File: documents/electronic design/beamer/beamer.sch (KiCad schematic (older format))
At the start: 25 parts, among them P1 CONN_01X20, P2 CONN_01X20, T1 2N7002K, T10 2N7002K, T2 2N7002K, T3 2N7002K, T4 2N7002K, T5 2N7002K, T6 2N7002K, T7 2N7002K, T8 2N7002K, T9 2N7002K, U1 NRF24L01-BRKOUT, U2 74HC595D

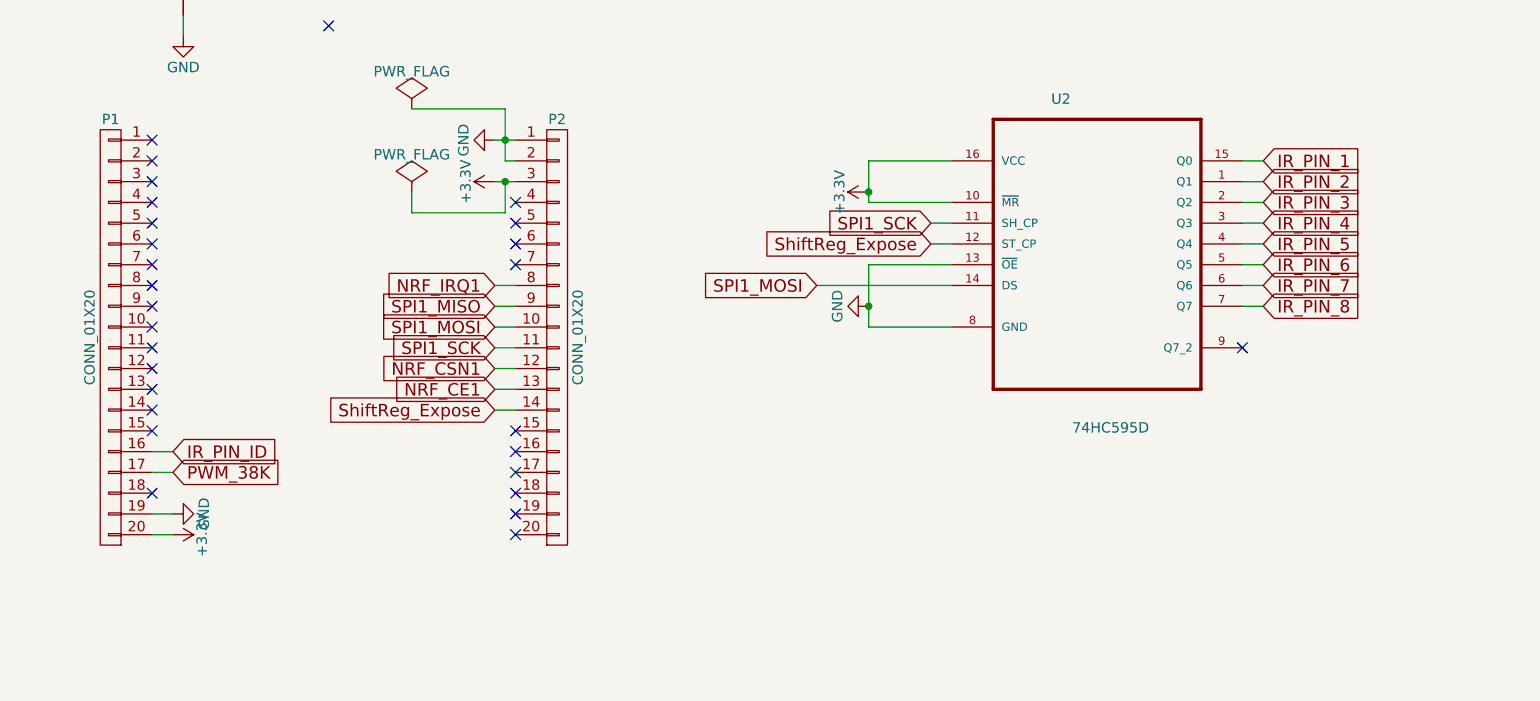
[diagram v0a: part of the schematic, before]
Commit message: update pcb for beamer with shift registar
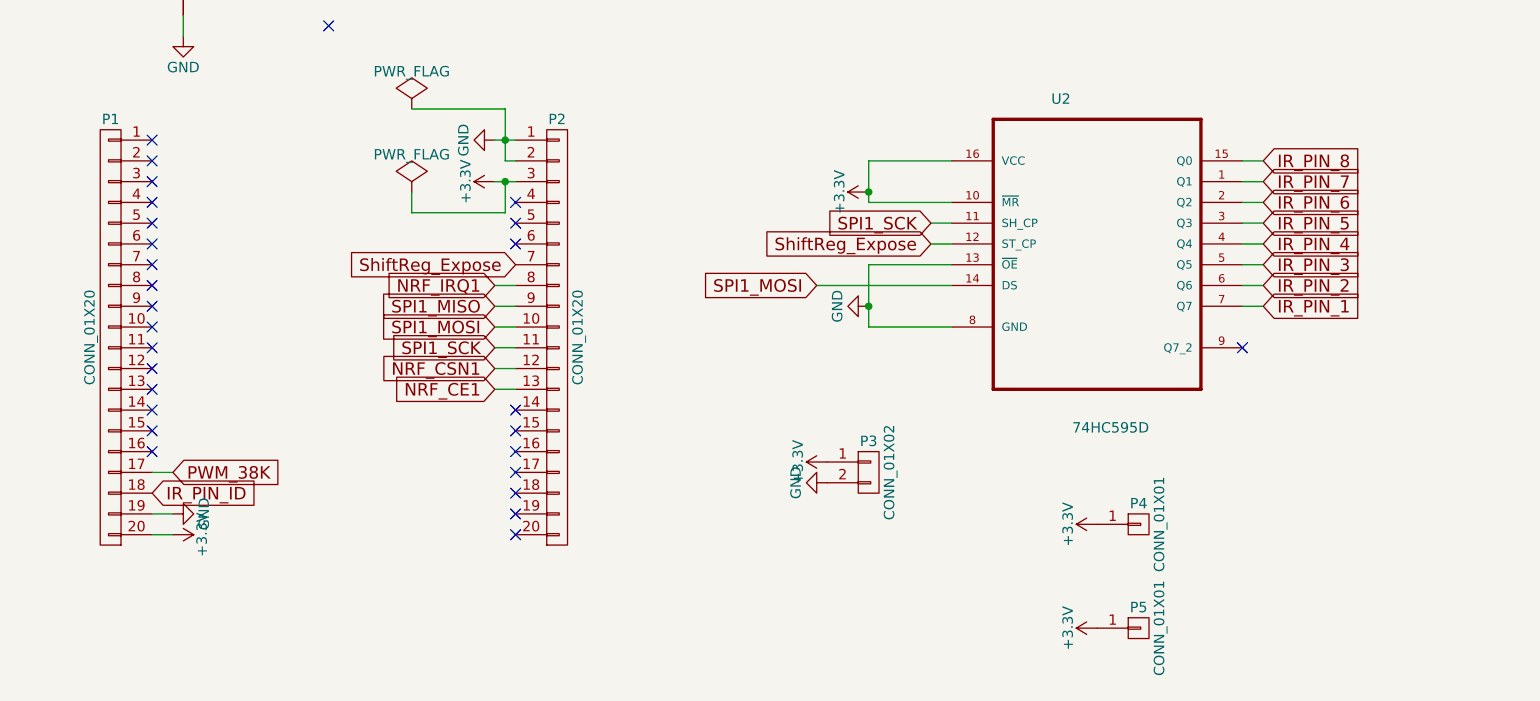
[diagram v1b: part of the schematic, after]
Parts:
- added P3: CONN_01X02, Pin_Headers:Pin_Header_Straight_1x02, symbol CONN_01X02
- added P4, P5: CONN_01X01, Pin_Headers:Pin_Header_Straight_1x01, symbol CONN_01X01
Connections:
- net +3V3: now also P3.1 (P1), P4.1 (P1), P5.1 (P1)
- net GND: now also P3.2 (P2)
- net IR_PIN_1: now also U2.7 (Q7); no longer U2.15 (Q0)
- net IR_PIN_2: now also U2.6 (Q6); no longer U2.1 (Q1)
- net IR_PIN_3: now also U2.5 (Q5); no longer U2.2 (Q2)
- net IR_PIN_4: now also U2.4 (Q4); no longer U2.3 (Q3)
- net IR_PIN_5: now also U2.3 (Q3); no longer U2.4 (Q4)
- net IR_PIN_6: now also U2.2 (Q2); no longer U2.5 (Q5)
- net IR_PIN_7: now also U2.1 (Q1); no longer U2.6 (Q6)
- net IR_PIN_8: now also U2.15 (Q0); no longer U2.7 (Q7)
- net IR_PIN_ID: now also P1.18 (P18); no longer P1.16 (P16)
- net ShiftReg_Expose: now also P2.7 (P7); no longer P2.14 (P14)
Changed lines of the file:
@@
 Text GLabel 4450 4300 0    60   Input ~ 0
 NRF_IRQ1
+Text GLabel 8150 4400 2    60   Input ~ 0
+IR_PIN_1
+Text GLabel 8150 4300 2    60   Input ~ 0
+IR_PIN_2
+Text GLabel 8150 4200 2    60   Input ~ 0
+IR_PIN_3
+Text GLabel 8150 4100 2    60   Input ~ 0
+IR_PIN_4
+Text GLabel 8150 4000 2    60   Input ~ 0
+IR_PIN_5
+Text GLabel 8150 3900 2    60   Input ~ 0
+IR_PIN_6
+Text GLabel 8150 3800 2    60   Input ~ 0
+IR_PIN_7
 Text GLabel 8150 3700 2    60   Input ~ 0
-IR_PIN_1
-Text GLabel 8150 3800 2    60   Input ~ 0
-IR_PIN_2
-Text GLabel 8150 3900 2    60   Input ~ 0
-IR_PIN_3
-Text GLabel 8150 4000 2    60   Input ~ 0
-IR_PIN_4
-Text GLabel 8150 4100 2    60   Input ~ 0
-IR_PIN_5
-Text GLabel 8150 4200 2    60   Input ~ 0
-IR_PIN_6
-Text GLabel 8150 4300 2    60   Input ~ 0
-IR_PIN_7
-Text GLabel 8150 4400 2    60   Input ~ 0
 IR_PIN_8
-Text GLabel 2900 5100 2    60   Input ~ 0
+Text GLabel 2800 5300 2    60   Input ~ 0
 IR_PIN_ID
-NoConn ~ 2800 5300
 NoConn ~ 2800 4200
 NoConn ~ 2800 4100
@@
 	1    0    0    -1
 $EndComp
-NoConn ~ 4550 4200
 NoConn ~ 2800 3600
 $Comp
@@
 	4450 3800 4550 3800
 Wire Wire Line
-	2800 5100 2900 5100
-Wire Wire Line
 	8050 4400 8150 4400
 Wire Wire Line
@@
 Wire Wire Line
 	6550 4000 6650 4000
-Text GLabel 4450 4900 0    60   Input ~ 0
+Text GLabel 4550 4200 0    60   Input ~ 0
 ShiftReg_Expose
 Text GLabel 6550 4100 0    60   Input ~ 0
@@
 NoConn ~ 4550 5100
 NoConn ~ 3650 3050
-Wire Wire Line
-	4550 4900 4450 4900
 NoConn ~ 2800 5000
+$Comp
+L CONN_01X02 P3
+U 1 1 57685656
+P 6250 5200
+F 0 "P3" H 6250 5350 50  0000 C CNN
+F 1 "CONN_01X02" V 6350 5200 50  0000 C CNN
+F 2 "Pin_Headers:Pin_Header_Straight_1x02" H 6250 5200 50  0001 C CNN
+F 3 "" H 6250 5200 50  0000 C CNN
+	1    6250 5200
+	1    0    0    -1
+$EndComp
+$Comp
+L +3.3V #PWR013
+U 1 1 5768570E
+P 6050 5150
+F 0 "#PWR013" H 6050 5000 50  0001 C CNN
+F 1 "+3.3V" H 6050 5290 50  0000 C CNN
+F 2 "" H 6050 5150 50  0000 C CNN
+F 3 "" H 6050 5150 50  0000 C CNN
+	1    6050 5150
+	0    -1   -1   0
+$EndComp
+$Comp
+L GND #PWR014
+U 1 1 57685767
+P 6050 5250
+F 0 "#PWR014" H 6050 5000 50  0001 C CNN
+F 1 "GND" H 6050 5100 50  0000 C CNN
+F 2 "" H 6050 5250 50  0000 C CNN
+F 3 "" H 6050 5250 50  0000 C CNN
+	1    6050 5250
+	0    1    1    0
+$EndComp
+NoConn ~ 4550 4900
+$Comp
+L CONN_01X01 P4
+U 1 1 5768633C
+P 7550 5450
+F 0 "P4" H 7550 5550 50  0000 C CNN
+F 1 "CONN_01X01" V 7650 5450 50  0000 C CNN
+F 2 "Pin_Headers:Pin_Header_Straight_1x01" H 7550 5450 50  0001 C CNN
+F 3 "" H 7550 5450 50  0000 C CNN
+	1    7550 5450
+	1    0    0    -1
+$EndComp
+$Comp
+L CONN_01X01 P5
+U 1 1 576863D4
+P 7550 5950
+F 0 "P5" H 7550 6050 50  0000 C CNN
+F 1 "CONN_01X01" V 7650 5950 50  0000 C CNN
+F 2 "Pin_Headers:Pin_Header_Straight_1x01" H 7550 5950 50  0001 C CNN
+F 3 "" H 7550 5950 50  0000 C CNN
+	1    7550 5950
+	1    0    0    -1
+$EndComp
+$Comp
+L +3.3V #PWR015
+U 1 1 5768645D
+P 7350 5450
+F 0 "#PWR015" H 7350 5300 50  0001 C CNN
+F 1 "+3.3V" H 7350 5590 50  0000 C CNN
+F 2 "" H 7350 5450 50  0000 C CNN
+F 3 "" H 7350 5450 50  0000 C CNN
+	1    7350 5450
+	0    -1   -1   0
+$EndComp
+$Comp
+L +3.3V #PWR016
+U 1 1 576864BF
+P 7350 5950
+F 0 "#PWR016" H 7350 5800 50  0001 C CNN
+F 1 "+3.3V" H 7350 6090 50  0000 C CNN
+F 2 "" H 7350 5950 50  0000 C CNN
+F 3 "" H 7350 5950 50  0000 C CNN
+	1    7350 5950
+	0    -1   -1   0
+$EndComp
+NoConn ~ 2800 5100
 $EndSCHEMATC

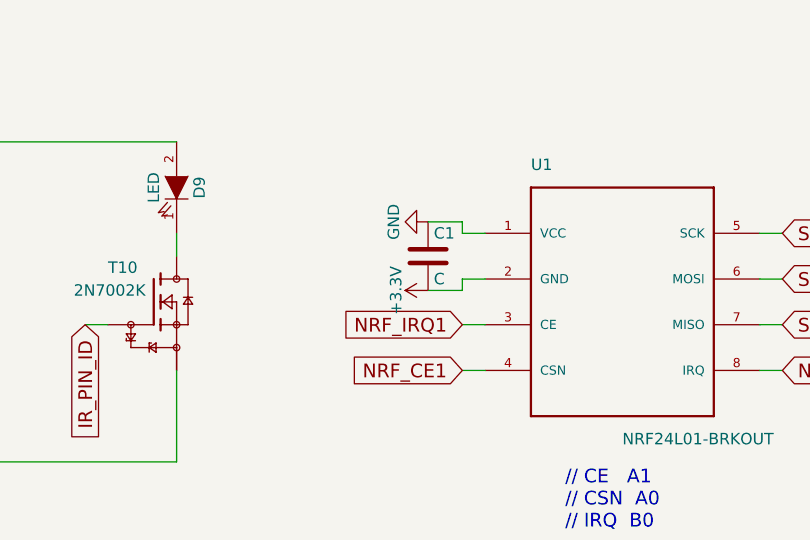
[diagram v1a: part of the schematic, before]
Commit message: update PCB for beamer, fix pin assignment for radiomodule
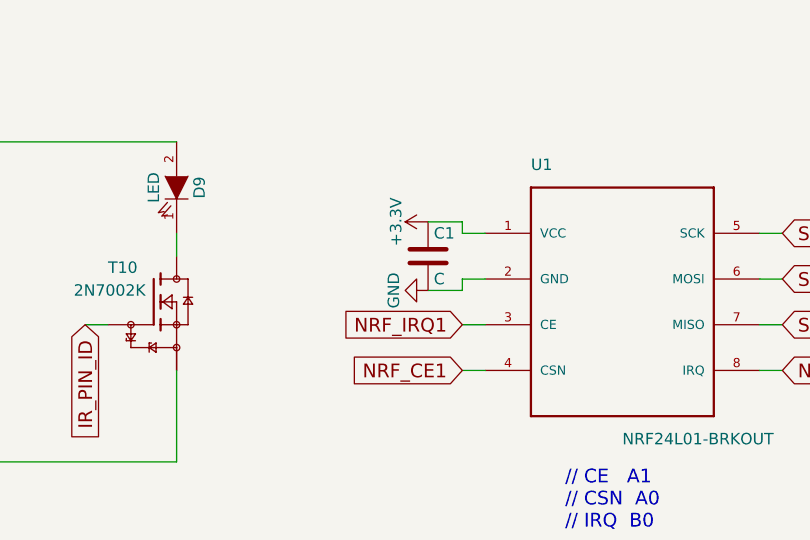
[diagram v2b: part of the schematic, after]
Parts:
- T1, T10, T2, T3, T4, T5, T6, T7, T8, T9: footprint sot23_modified:SOT23Mod -> sot23_modified:SOT23
- U1: footprint se8r01_smd:SE8R01_SMD -> NRF24L01-BRKOUT:NRF24L01-BKKOUT
- U2: footprint SOIC127P1030X265-16N:SOIC127P1030X265-16N -> 74HC595:SO16
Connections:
- net +3V3: now also C1.1, U1.1 (VCC); no longer C1.2, U1.2 (GND)
- net GND: now also C1.2, U1.2 (GND); no longer C1.1, U1.1 (VCC)
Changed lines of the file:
@@
 LIBS:conn_R
 LIBS:2N7002K
-LIBS:74HC595D
+LIBS:74HC595
 LIBS:beamer-cache
 EELAYER 25 0
@@
 F 0 "T1" H 1150 2150 50  0000 L CNN
 F 1 "2N7002K" H 1000 2050 50  0000 L CNN
-F 2 "sot23_modified:SOT23Mod" H 1350 1900 50  0001 L CNN
+F 2 "sot23_modified:SOT23" H 1350 1900 50  0001 L CNN
 F 3 "" H 1350 1900 60  0000 C CNN
 	1    1350 1900
@@
 F 0 "T4" H 2650 3050 50  0000 L CNN
 F 1 "2N7002K" H 2500 2950 50  0000 L CNN
-F 2 "sot23_modified:SOT23Mod" H 2850 2800 50  0001 L CNN
+F 2 "sot23_modified:SOT23" H 2850 2800 50  0001 L CNN
 F 3 "" H 2850 2800 60  0000 C CNN
 	1    2850 2800
@@
 F 0 "T2" H 1750 2150 50  0000 L CNN
 F 1 "2N7002K" H 1600 2050 50  0000 L CNN
-F 2 "sot23_modified:SOT23Mod" H 1950 1900 50  0001 L CNN
+F 2 "sot23_modified:SOT23" H 1950 1900 50  0001 L CNN
 F 3 "" H 1950 1900 60  0000 C CNN
 	1    1950 1900
@@
 F 0 "T3" H 2350 2150 50  0000 L CNN
 F 1 "2N7002K" H 2200 2050 50  0000 L CNN
-F 2 "sot23_modified:SOT23Mod" H 2550 1900 50  0001 L CNN
+F 2 "sot23_modified:SOT23" H 2550 1900 50  0001 L CNN
 F 3 "" H 2550 1900 60  0000 C CNN
 	1    2550 1900
@@
 F 0 "T5" H 2950 2150 50  0000 L CNN
 F 1 "2N7002K" H 2800 2050 50  0000 L CNN
-F 2 "sot23_modified:SOT23Mod" H 3150 1900 50  0001 L CNN
+F 2 "sot23_modified:SOT23" H 3150 1900 50  0001 L CNN
 F 3 "" H 3150 1900 60  0000 C CNN
 	1    3150 1900
@@
 F 0 "T6" H 3550 2150 50  0000 L CNN
 F 1 "2N7002K" H 3400 2050 50  0000 L CNN
-F 2 "sot23_modified:SOT23Mod" H 3750 1900 50  0001 L CNN
+F 2 "sot23_modified:SOT23" H 3750 1900 50  0001 L CNN
 F 3 "" H 3750 1900 60  0000 C CNN
 	1    3750 1900
@@
 F 0 "T7" H 4150 2150 50  0000 L CNN
 F 1 "2N7002K" H 4000 2050 50  0000 L CNN
-F 2 "sot23_modified:SOT23Mod" H 4350 1900 50  0001 L CNN
+F 2 "sot23_modified:SOT23" H 4350 1900 50  0001 L CNN
 F 3 "" H 4350 1900 60  0000 C CNN
 	1    4350 1900
@@
 F 0 "T8" H 4750 2150 50  0000 L CNN
 F 1 "2N7002K" H 4600 2050 50  0000 L CNN
-F 2 "sot23_modified:SOT23Mod" H 4950 1900 50  0001 L CNN
+F 2 "sot23_modified:SOT23" H 4950 1900 50  0001 L CNN
 F 3 "" H 4950 1900 60  0000 C CNN
 	1    4950 1900
@@
 F 0 "T9" H 5350 2150 50  0000 L CNN
 F 1 "2N7002K" H 5200 2050 50  0000 L CNN
-F 2 "sot23_modified:SOT23Mod" H 5550 1900 50  0001 L CNN
+F 2 "sot23_modified:SOT23" H 5550 1900 50  0001 L CNN
 F 3 "" H 5550 1900 60  0000 C CNN
 	1    5550 1900
@@
 F 0 "T10" H 6600 2150 50  0000 L CNN
 F 1 "2N7002K" H 6450 2050 50  0000 L CNN
-F 2 "sot23_modified:SOT23Mod" H 6800 1900 50  0001 L CNN
+F 2 "sot23_modified:SOT23" H 6800 1900 50  0001 L CNN
 F 3 "" H 6800 1900 60  0000 C CNN
 	1    6800 1900
@@
 L GND #PWR05
 U 1 1 57142C4E
+P 8000 1750
+F 0 "#PWR05" H 8000 1500 50  0001 C CNN
+F 1 "GND" H 8000 1600 50  0000 C CNN
+F 2 "" H 8000 1750 50  0000 C CNN
+F 3 "" H 8000 1750 50  0000 C CNN
+	1    8000 1750
+	0    1    1    0
+$EndComp
+$Comp
+L +3.3V #PWR06
+U 1 1 57142CA4
 P 8000 1450
-F 0 "#PWR05" H 8000 1200 50  0001 C CNN
-F 1 "GND" H 8000 1300 50  0000 C CNN
+F 0 "#PWR06" H 8000 1300 50  0001 C CNN
+F 1 "+3.3V" H 8000 1590 50  0000 C CNN
 F 2 "" H 8000 1450 50  0000 C CNN
 F 3 "" H 8000 1450 50  0000 C CNN
 	1    8000 1450
-	0    1    1    0
-$EndComp
-$Comp
-L +3.3V #PWR06
-U 1 1 57142CA4
-P 8000 1750
-F 0 "#PWR06" H 8000 1600 50  0001 C CNN
-F 1 "+3.3V" H 8000 1890 50  0000 C CNN
-F 2 "" H 8000 1750 50  0000 C CNN
-F 3 "" H 8000 1750 50  0000 C CNN
-	1    8000 1750
 	0    -1   -1   0
-$EndComp
-$Comp
-L NRF24L01-BRKOUT U1
-U 1 1 5713E8BE
-P 8850 1800
-F 0 "U1" H 8450 2400 50  0000 L CNN
-F 1 "NRF24L01-BRKOUT" H 8850 1200 50  0000 L CNN
-F 2 "se8r01_smd:SE8R01_SMD" H 8850 1800 50  0001 L CNN
-F 3 "" H 8850 1800 60  0000 C CNN
-	1    8850 1800
-	1    0    0    -1
 $EndComp
 NoConn ~ 2800 3600
@@
 F 0 "U2" H 7129 4598 50  0000 L CNN
 F 1 "74HC595D" H 7230 3015 50  0000 L CNN
-F 2 "SOIC127P1030X265-16N:SOIC127P1030X265-16N" H 7350 4000 50  0001 L CNN
+F 2 "74HC595:SO16" H 7350 4000 50  0001 L CNN
 F 3 "" H 7350 4000 60  0000 C CNN
 	1    7350 4000
@@
 $EndComp
 NoConn ~ 2800 5100
+$Comp
+L NRF24L01-BRKOUT U1
+U 1 1 576CC048
+P 8850 1800
+F 0 "U1" H 8450 2400 50  0000 L CNN
+F 1 "NRF24L01-BRKOUT" H 8850 1200 50  0000 L CNN
+F 2 "NRF24L01-BRKOUT:NRF24L01-BKKOUT" H 8850 1800 50  0001 L CNN
+F 3 "" H 8850 1800 60  0000 C CNN
+	1    8850 1800
+	1    0    0    -1
+$EndComp
 $EndSCHEMATC

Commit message: minor update in beamer pcb layout
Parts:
- U1: symbol NRF24L01-BRKOUT -> NRF24L01-BRKOUT-RESCUE-beamer
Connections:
- net NRF_CE1: now also U1.3 (CE); no longer U1.4 (CSN)
- net NRF_CSN1: now also U1.4 (CSN); no longer U1.8 (IRQ)
- net NRF_IRQ1: now also U1.8 (IRQ); no longer U1.3 (CE)
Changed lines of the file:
@@
 EESchema Schematic File Version 2
+LIBS:beamer-rescue
 LIBS:power
 LIBS:device
@@
 NoConn ~ 2800 5100
 $Comp
-L NRF24L01-BRKOUT U1
+L NRF24L01-BRKOUT-RESCUE-beamer U1
 U 1 1 576CC048
 P 8850 1800

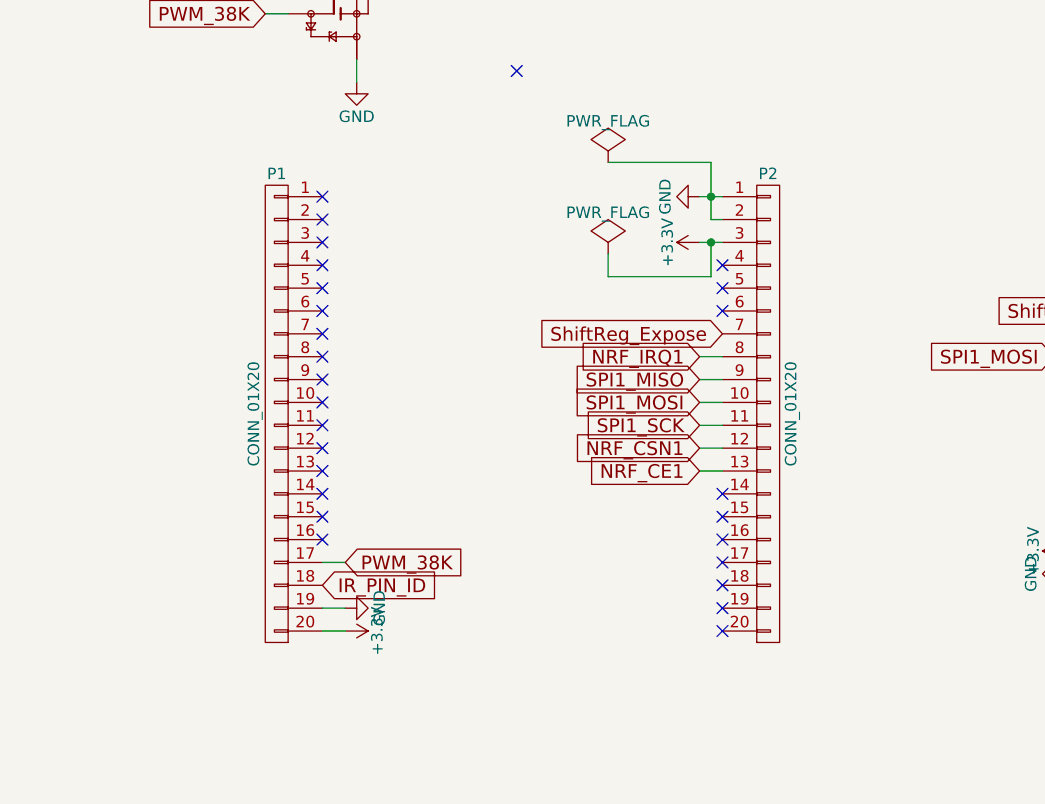
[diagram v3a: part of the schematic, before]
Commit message: update PCB for beamer
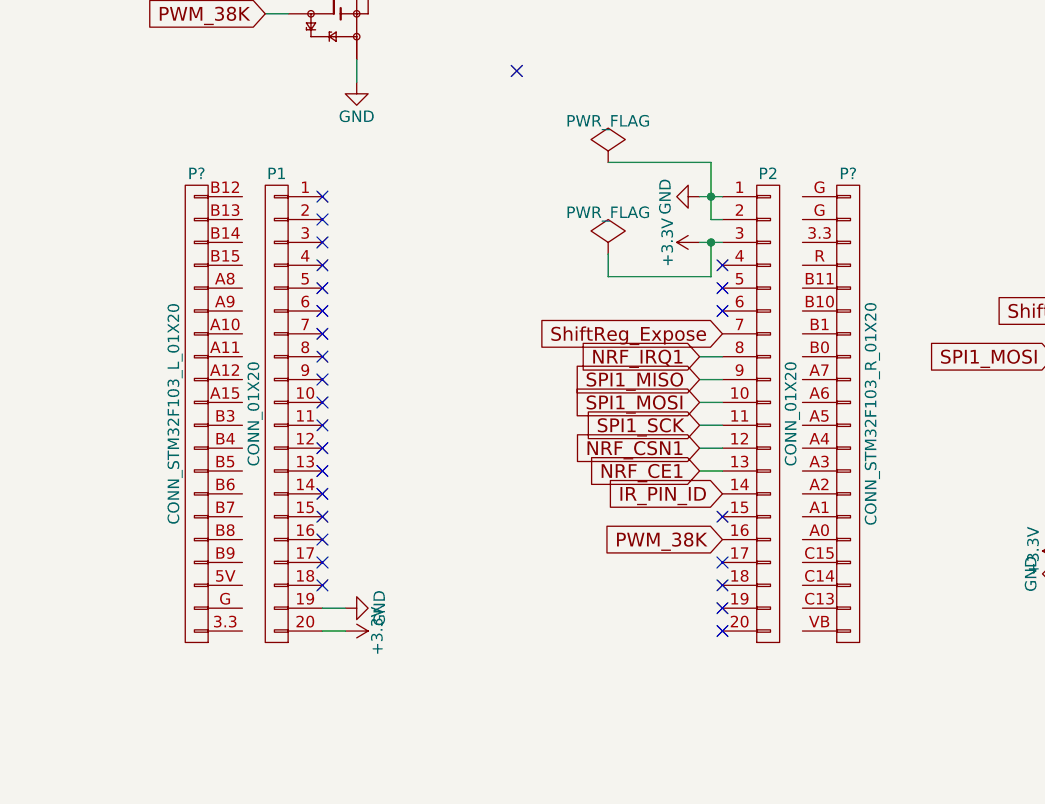
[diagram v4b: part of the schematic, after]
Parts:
- added P?: CONN_STM32F103_R_01X20, symbol CONN_STM32F103_R_01X20
- added P?: CONN_STM32F103_L_01X20, symbol CONN_STM32F103_L_01X20
- U1: footprint NRF24L01-BRKOUT:NRF24L01-BKKOUT -> SE8R01:se8r01_smd
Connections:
- net IR_PIN_ID: now also P2.14 (P14); no longer P1.18 (P18)
- net PWM_38K: now also P2.16 (P16); no longer P1.17 (P17)
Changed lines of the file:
@@
 Text GLabel 8150 3700 2    60   Input ~ 0
 IR_PIN_8
-Text GLabel 2800 5300 2    60   Input ~ 0
-IR_PIN_ID
 NoConn ~ 2800 4200
 NoConn ~ 2800 4100
@@
 	0    -1   -1   0
 $EndComp
-Text GLabel 2900 5200 2    60   Input ~ 0
+Text GLabel 4550 5100 0    60   Input ~ 0
 PWM_38K
 $Comp
@@
 Connection ~ 4500 3600
 Wire Wire Line
-	2800 5200 2900 5200
-Wire Wire Line
 	4450 3600 4550 3600
 Wire Wire Line
@@
 NoConn ~ 4550 5300
 NoConn ~ 4550 5200
-NoConn ~ 4550 5100
+NoConn ~ 2800 5200
 NoConn ~ 3650 3050
 NoConn ~ 2800 5000
@@
 	0    1    1    0
 $EndComp
-NoConn ~ 4550 4900
+NoConn ~ 2800 5300
 $Comp
 L CONN_01X01 P4
@@
 F 0 "U1" H 8450 2400 50  0000 L CNN
 F 1 "NRF24L01-BRKOUT" H 8850 1200 50  0000 L CNN
-F 2 "NRF24L01-BRKOUT:NRF24L01-BKKOUT" H 8850 1800 50  0001 L CNN
+F 2 "SE8R01:se8r01_smd" H 8850 1800 50  0001 L CNN
 F 3 "" H 8850 1800 60  0000 C CNN
 	1    8850 1800
 	1    0    0    -1
 $EndComp
+Text GLabel 4550 4900 0    60   Input ~ 0
+IR_PIN_ID
+$Comp
+L CONN_STM32F103_L_01X20 P?
+U 1 1 5770F34D
+P 2250 4550
+F 0 "P?" H 2250 5600 50  0000 C CNN
+F 1 "CONN_STM32F103_L_01X20" V 2350 4550 50  0000 C CNN
+F 2 "" H 2250 4550 50  0000 C CNN
+F 3 "" H 2250 4550 50  0000 C CNN
+	1    2250 4550
+	-1   0    0    -1
+$EndComp
+$Comp
+L CONN_STM32F103_R_01X20 P?
+U 1 1 5770F25B
+P 5100 4550
+F 0 "P?" H 5100 5600 50  0000 C CNN
+F 1 "CONN_STM32F103_R_01X20" V 5200 4550 50  0000 C CNN
+F 2 "" H 5100 4550 50  0000 C CNN
+F 3 "" H 5100 4550 50  0000 C CNN
+	1    5100 4550
+	1    0    0    -1
+$EndComp
